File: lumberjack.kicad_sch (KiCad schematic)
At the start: 159 parts, among them J1 USB, J2 AVR_ISP_6, J3 JST, J4 JST, SW1 RESET, SW2 BOOT, U1 ATMEGA328-PU, Y1 16MHz

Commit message: Switch to SMD USB-C connector
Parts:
- J1: footprint Connector_USB:USB_C_Receptacle_GCT_USB4085 -> lumberjack:TYPE-C-31-M-12
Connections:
- no-connect marks 1 -> 3
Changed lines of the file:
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@@
   (junction (at 137.16 39.37) (diameter 0) (color 0 0 0 0)
   )
+  (no_connect (at 44.45 63.5))
+  (no_connect (at 44.45 66.04))
   (no_connect (at 35.56 111.76))
   (wire (pts (xy 81.28 167.64) (xy 81.28 187.96))
@@
     (property "Reference" "J1" (id 0) (at 31.9278 28.7782 0))
     (property "Value" "USB" (id 1) (at 31.9278 31.0896 0))
-    (property "Footprint" "Connector_USB:USB_C_Receptacle_GCT_USB4085" (id 2) (at 33.02 50.8 0)
+    (property "Footprint" "lumberjack:TYPE-C-31-M-12" (id 2) (at 33.02 50.8 0)
       (effects (font (size 1.27 1.27)) hide)
     )
@@
     )
     (path "/00000000-0000-0000-0000-0000601e2e5d"
-      (reference "J1") (unit 1) (value "USB") (footprint "Connector_USB:USB_C_Receptacle_GCT_USB4085")
+      (reference "J1") (unit 1) (value "USB") (footprint "lumberjack:TYPE-C-31-M-12")
     )
     (path "/00000000-0000-0000-0000-00005c3f2fd0"

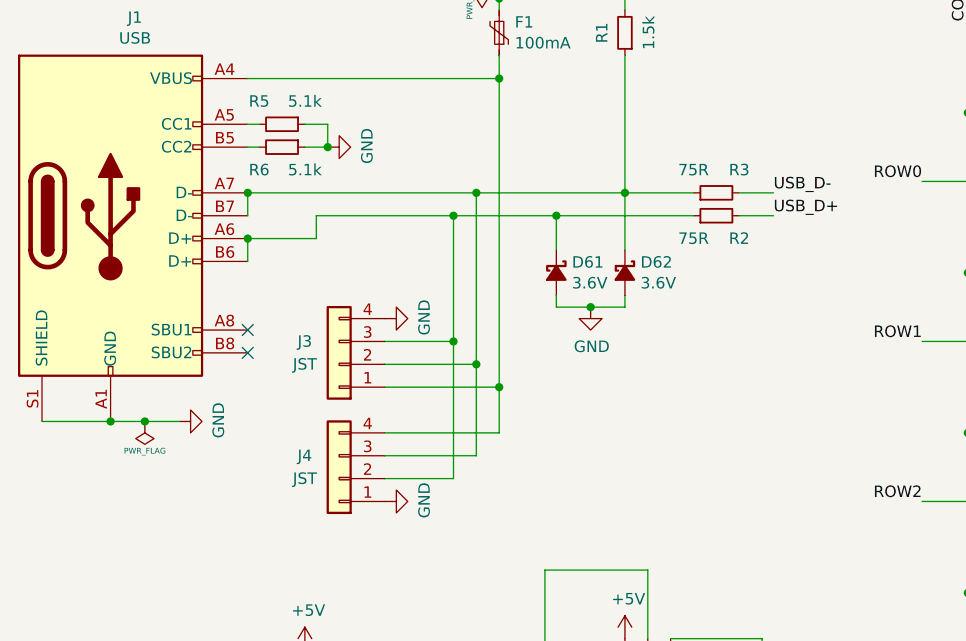
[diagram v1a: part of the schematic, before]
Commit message: Add Molex connector footprint
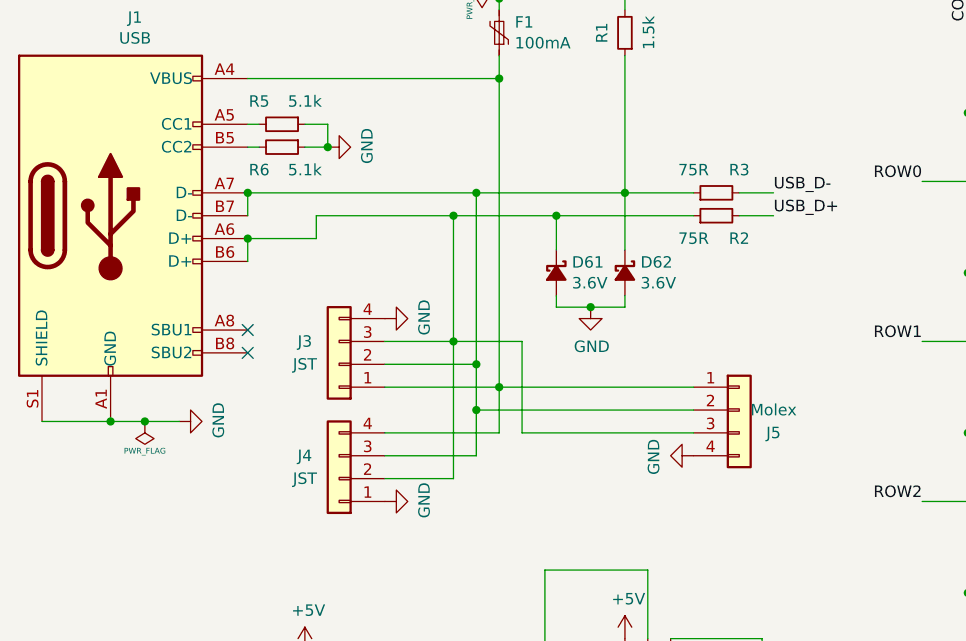
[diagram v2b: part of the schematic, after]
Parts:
- added J5: Molex, lumberjack:PicoEZMate-Reinforced-Lite, symbol Connector_Generic:Conn_01x04
- MX1, MX10, MX11, MX12, MX13, MX14, MX15, MX16, MX17, MX18, MX19, MX2, MX20, MX21, MX22, MX23, MX24, MX25, MX26, MX27, MX28, MX29, MX3, MX30, MX31, MX32, MX33, MX34, MX35, MX36, MX37, MX38, MX39, MX4, MX40, MX41, MX42, MX43, MX44, MX45, MX46, MX47, MX48, MX49, MX5, MX50, MX51, MX52, MX53, MX54, MX55, MX56, MX57, MX58, MX59, MX6, MX60, MX7, MX9: footprint lumberjack:MX_Alps_Choc -> lumberjack:MX
- MX8: footprint lumberjack:MX_Alps_Choc_NTHSTH -> lumberjack:MX_NTHSTH
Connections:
- net GND: now also J5.4 (Pin_4)
- net at D61.1 (K), J1.A6 (D+), J1.B6 (D+)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: now also J5.3 (Pin_3)
- net at D62.1 (K), J1.A7 (D-), J1.B7 (D-)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: now also J5.2 (Pin_2)
- net at F1.1, J1.A4 (VBUS), J1.A9 (VBUS)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: now also J5.1 (Pin_1)
